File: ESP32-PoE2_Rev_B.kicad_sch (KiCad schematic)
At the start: 120 parts, among them IC1 SI4435DYPBF, IC2 SI4435DYPBF, IC3 KTA1170GVAE-TB, J1 B3B-XH-A, J2 ARJM11D7-114-AB-EW2, U1 TPS2378DDAR(HSOIC-8), U2 LMR33630ADDAR, U3 TX4138(ESOIC-8), U4 TX4138(ESOIC-8), U5 AP62201Z6-7, U6 AP62201Z6-7, U7 W5500

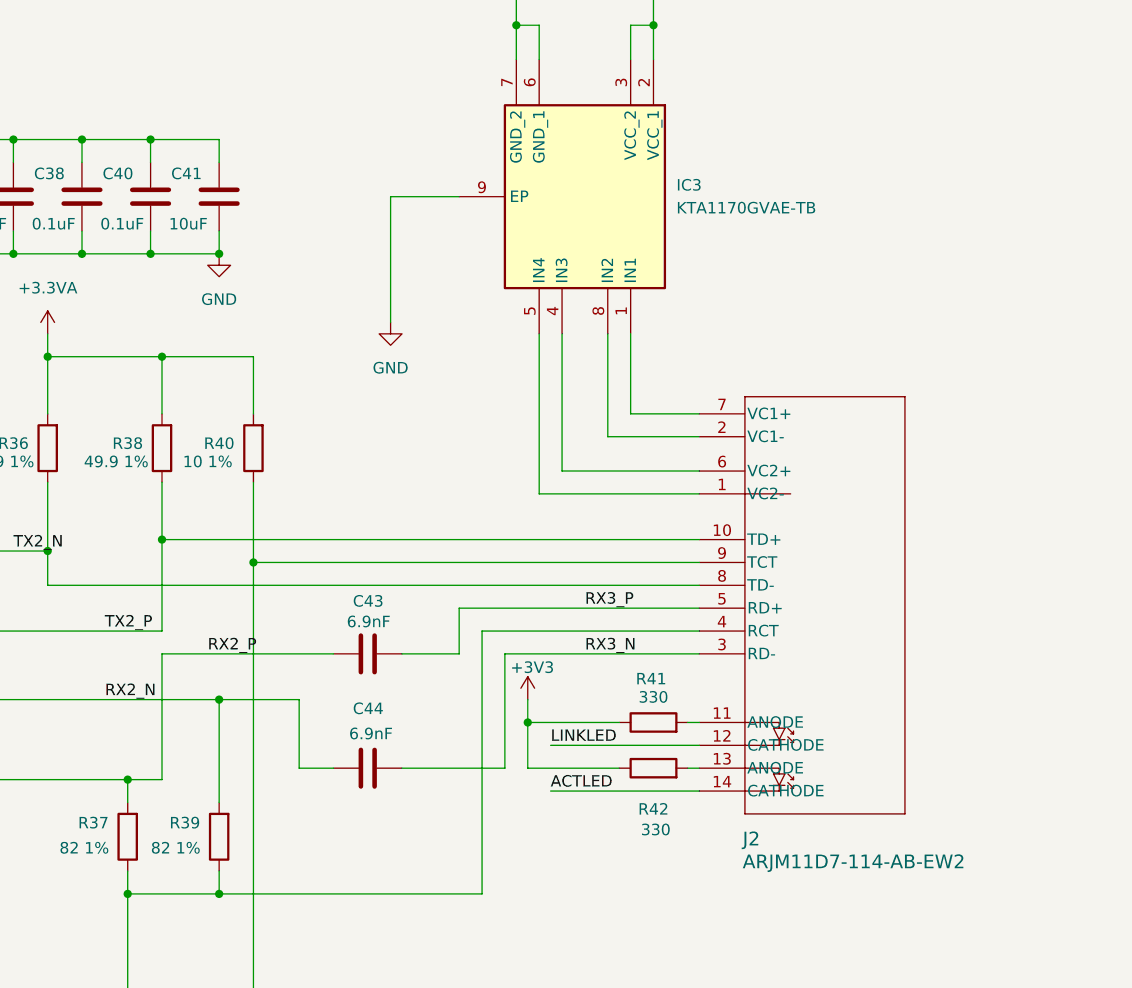
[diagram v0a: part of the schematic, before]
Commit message: WIP - starting moving reference silkscreens around
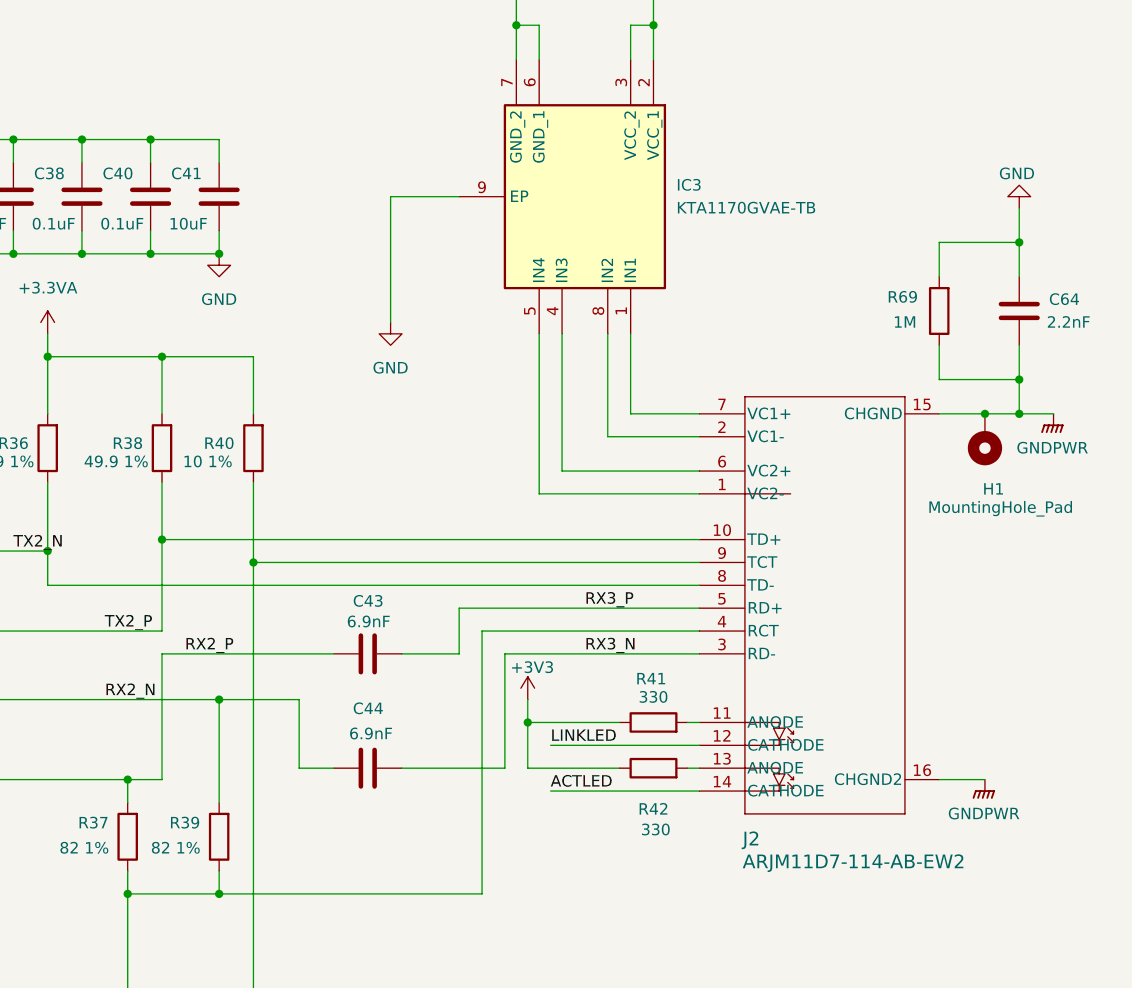
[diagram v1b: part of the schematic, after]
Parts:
- added C64: 2.2nF, Capacitor_SMD:C_1812_4532Metric, symbol Device:C
- added H1: MountingHole_Pad, MountingHole:MountingHole_3mm_Pad_TopOnly, symbol Mechanical:MountingHole_Pad
- added R69: 1M, Resistor_SMD:R_1206_3216Metric, symbol Device:R
- J2: footprint ARJM11D7_114_AB_EW2:CONN_ARJM11D7-114-AB-EW2_ABR -> CONN_ARJM11D7-114-AB-EW2_ABR
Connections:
- net GND: now also C64.1, R69.2
- new net GNDPWR: C64.2, H1.1, J2.15 (CHGND), J2.16 (CHGND2), R69.1
